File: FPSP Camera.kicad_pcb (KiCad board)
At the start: 4 copper layers, 168.1 x 35 mm, 81 parts, among them J2 Conn_01x02_Pin, J3 USB_B_Micro, J4 SM03B-SRSS-TB, J5 Conn_01x24_Socket, J6 Conn_02x06_Odd_Even, SW1 SW_Push, SW2 SW_Push, U1 RP2350_60QFN, U2 W25Q128JVS, U3 ASM330LHHXTR, U5 TLV74328_SOT23-5, U6 TLV74315_SOT23-5, U7 SiT2001B, U8 NCP1117-3.3_SOT223

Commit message: pcb update
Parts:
- moved D2 19.7 mm to (22.7, 32.2), turned to 0 degrees
- moved D3 17.8 mm to (22.7, 35.2), turned to 0 degrees
- moved C15 16.8 mm to (85.9, 27.2), turned to 90 degrees
- moved J4 16.5 mm to (85.5, 46.5)
- moved TP2 14.5 mm to (82.7, 22.5)
- moved R20 14.4 mm to (26.0, 32.2), turned to 180 degrees
- moved J6 13.9 mm to (48.0, 45.5), turned to -90 degrees
- moved D1 13.8 mm to (22.8, 29.2), turned to 0 degrees
- moved R21 12.7 mm to (26.0, 35.2), turned to 180 degrees
- moved TP1 12.4 mm to (65.7, 44.0)
- moved R18 10.9 mm to (26.0, 29.2), turned to 180 degrees
- moved C31 10.3 mm to (30.7, 37.9)
- moved R2 9.57 mm to (74.7, 17.2)
- moved R6 9.50 mm to (76.4, 17.2)
- moved C14 9.16 mm to (71.9, 36.5), turned to 180 degrees
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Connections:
- U1 pad 16: DATA2_1 -> DATA9_1
- U1 pad 17: DATA3_1 -> DATA8_1
- U1 pad 18: DATA4_1 -> DATA7_1
- U1 pad 19: DATA5_1 -> DATA6_1
- U1 pad 27: DATA6_1 -> DATA2_1
- U1 pad 28: DATA7_1 -> DATA5_1
- U1 pad 29: DATA8_1 -> DATA3_1
- U1 pad 31: DATA9_1 -> DATA4_1
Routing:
- net +3.3V: track 0.00 -> 114.9 mm
- net SDO_imu_1: track 0.00 -> 42.0 mm, vias 0 -> 2
- net SDA_imu_1: track 0.00 -> 40.3 mm, vias 0 -> 4
- net INT1_1: track 0.00 -> 35.9 mm
- net /IOs/XCLK: track 0.00 -> 35.6 mm, vias 0 -> 1
- net SCL_imu_1: track 0.00 -> 35.6 mm, vias 0 -> 2
- net DATA4_1: track 0.00 -> 35.0 mm, vias 0 -> 1
- net INT2_1: track 0.00 -> 33.7 mm, vias 0 -> 2
- net CS_1: track 0.00 -> 33.2 mm
- net HSYNC_1: track 0.00 -> 33.1 mm, vias 0 -> 3
- net DATA5_1: track 0.00 -> 33.1 mm, vias 0 -> 1
- net DATA3_1: track 0.00 -> 33.0 mm, vias 0 -> 1
- net DATA2_1: track 0.00 -> 32.7 mm, vias 0 -> 1
- net +2V8: track 0.00 -> 27.5 mm, vias 0 -> 2
- net DATA6_1: track 0.00 -> 26.9 mm, vias 0 -> 1
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- added copper zone on F.Cu, net +3.3V
- added copper zone on F.Cu, net +5V
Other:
- board text added: "1.5"
- board text added: "2.8"
- board text added: "3.3"
- board text added: "5.0"

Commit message: finished the routing
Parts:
- removed C17: 100n, Capacitor_SMD:C_0603_1608Metric_Pad1.08x0.95mm_HandSolder
- moved J6 12.9 mm to (35.5, 48.2), turned to 90 degrees
- moved TP1 0.50 mm to (65.7, 43.5)
- moved TP2 0.50 mm to (82.7, 23.0)
- moved C21 0.40 mm to (56.0, 38.8)
- moved R13 0.40 mm to (56.0, 36.8)
- moved J3 0.31 mm to (91.0, 16.9)
- moved C35 0.25 mm to (56.0, 40.8)
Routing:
- net +3.3V: track 114.9 -> 266.2 mm, vias 0 -> 12
- net POSITION_OUT_1: track 0.00 -> 58.9 mm, vias 0 -> 1
- net IMAGE_OUT_1_1: track 0.00 -> 58.5 mm, vias 0 -> 1
- net IMAGE_OUT_2_1: track 0.00 -> 57.4 mm, vias 0 -> 1
- net /MCU/FLASH_SS_1: track 12.7 -> 32.1 mm, vias 0 -> 2
- net +1V1: track 26.7 -> 44.6 mm
- net +1V5: track 21.2 -> 37.1 mm, vias 2 -> 3
- net +2V8: track 27.5 -> 43.2 mm, vias 2 -> 3
- net /MCU/QSPI_SS_1: track 1.70 -> 15.7 mm, vias 0 -> 2
- net ~{RESET_1}: track 20.5 -> 25.7 mm, vias 1 -> 2
- net /IOs/PWDN_1: track 0.00 -> 5.12 mm, vias 0 -> 1
- net DATA1_1: track 0.00 -> 5.09 mm, vias 0 -> 1
- net PCLK_1: track 22.0 -> 26.0 mm, vias 1 -> 2
- net Net-(J5-Pin_1): track 0.00 -> 3.98 mm, vias 0 -> 1
- net DATA5_1: track 33.1 -> 30.7 mm
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- added copper zone on B.Cu, net GND
- added copper zone on F.Cu, net GND

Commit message: layout details finalized for prototype
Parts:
- moved H3 82.6 mm to (99.9, 46.5)
- moved H2 82.2 mm to (99.8, 18.5)
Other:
- board size 168.1 x 35 mm -> 85.7 x 35 mm
- board text added: "FPSP v1.0 Junyuan Zheng Junzhe Chen"
- board text added: "GND"
- board text added: "Img1|Img2|Pos"
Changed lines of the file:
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@@
 		(tags "capacitor handsolder")
 		(property "Reference" "C35"
-			(at 3.4375 -0.05 0)
+			(at 3.2375 -0.2 0)
 			(layer "F.SilkS")
 			(effects
@@
 	(footprint "MountingHole:MountingHole_2.7mm_M2.5"
 		(layer "F.Cu")
-		(at 182.45 46.6)
+		(at 99.9 46.5)
 		(descr "Mounting Hole 2.7mm, M2.5, no annular, generated by kicad-footprint-generator mountinghole.py")
 		(tags "mountinghole M2.5")
@@
 	(footprint "MountingHole:MountingHole_2.7mm_M2.5"
 		(layer "F.Cu")
-		(at 181.95 18.9)
+		(at 99.8 18.5)
 		(descr "Mounting Hole 2.7mm, M2.5, no annular, generated by kicad-footprint-generator mountinghole.py")
 		(tags "mountinghole M2.5")
@@
 		(tags "capacitor handsolder")
 		(property "Reference" "C30"
-			(at 0 -2.9 90)
+			(at 0 -1.7125 90)
 			(layer "F.SilkS")
 			(effects
@@
 		(tags "Through hole pin header THT 2x06 2.54mm double row")
 		(property "Reference" "J6"
-			(at 1.27 -2.38 90)
+			(at 0.9 15.35 90)
 			(layer "F.SilkS")
+			(hide yes)
 			(effects
 				(font
@@
 			(at 0 0 0)
 			(layer "F.SilkS")
+			(hide yes)
 			(effects
 				(font
@@
 			(at 0 0 270)
 			(layer "F.SilkS")
+			(hide yes)
 			(effects
 				(font
@@
 		)
 	)
+	(gr_line
+		(start 47.25 43)
+		(end 38.3 44.05)
+		(stroke
+			(width 0.13)
+			(type solid)
+		)
+		(layer "F.SilkS")
+	)
+	(gr_line
+		(start 51.3 42.85)
+		(end 40.65 44.1)
+		(stroke
+			(width 0.13)
+			(type solid)
+		)
+		(layer "F.SilkS")
+	)
+	(gr_line
+		(start 43.35 42.85)
+		(end 35.55 44.1)
+		(stroke
+			(width 0.13)
+			(type solid)
+		)
+		(layer "F.SilkS")
+	)
 	(gr_rect
 		(start 17.7 15)
-		(end 185.848 50)
+		(end 103.424 50)
 		(stroke
 			(width 0.2)
@@
 		(layer "Edge.Cuts")
 	)
+	(gr_text "Img1|Img2|Pos"
+		(at 42.9 42.7 0)
+		(layer "F.SilkS")
+		(effects
+			(font
+				(size 0.8 0.8)
+				(thickness 0.15)
+				(bold yes)
+			)
+			(justify left bottom)
+		)
+	)
 	(gr_text "1.5"
 		(at 17.88 35.95 0)
@@
 		)
 	)
+	(gr_text "GND"
+		(at 50.1 46.2 0)
+		(layer "F.SilkS")
+		(effects
+			(font
+				(size 0.8 0.8)
+				(thickness 0.15)
+				(bold yes)
+			)
+			(justify left bottom)
+		)
+	)
 	(gr_text "1V1"
 		(at 78.7 23 0)
@@
 		)
 	)
+	(gr_text "FPSP v1.0\nJunyuan Zheng\nJunzhe Chen\n"
+		(at 101.65 38.9 90)
+		(layer "F.SilkS")
+		(effects
+			(font
+				(size 1 1)
+				(thickness 0.25)
+				(bold yes)
+			)
+			(justify left bottom)
+		)
+	)
 	(gr_text "3.3"
 		(at 17.98 29.95 0)
@@
 		(polygon
 			(pts
-				(xy 17.7 15) (xy 17.7 50) (xy 96.7 50) (xy 96.7 15)
+				(xy 17.7 15) (xy 17.7 50) (xy 103.426 50) (xy 103.426 15)
 			)
 		)

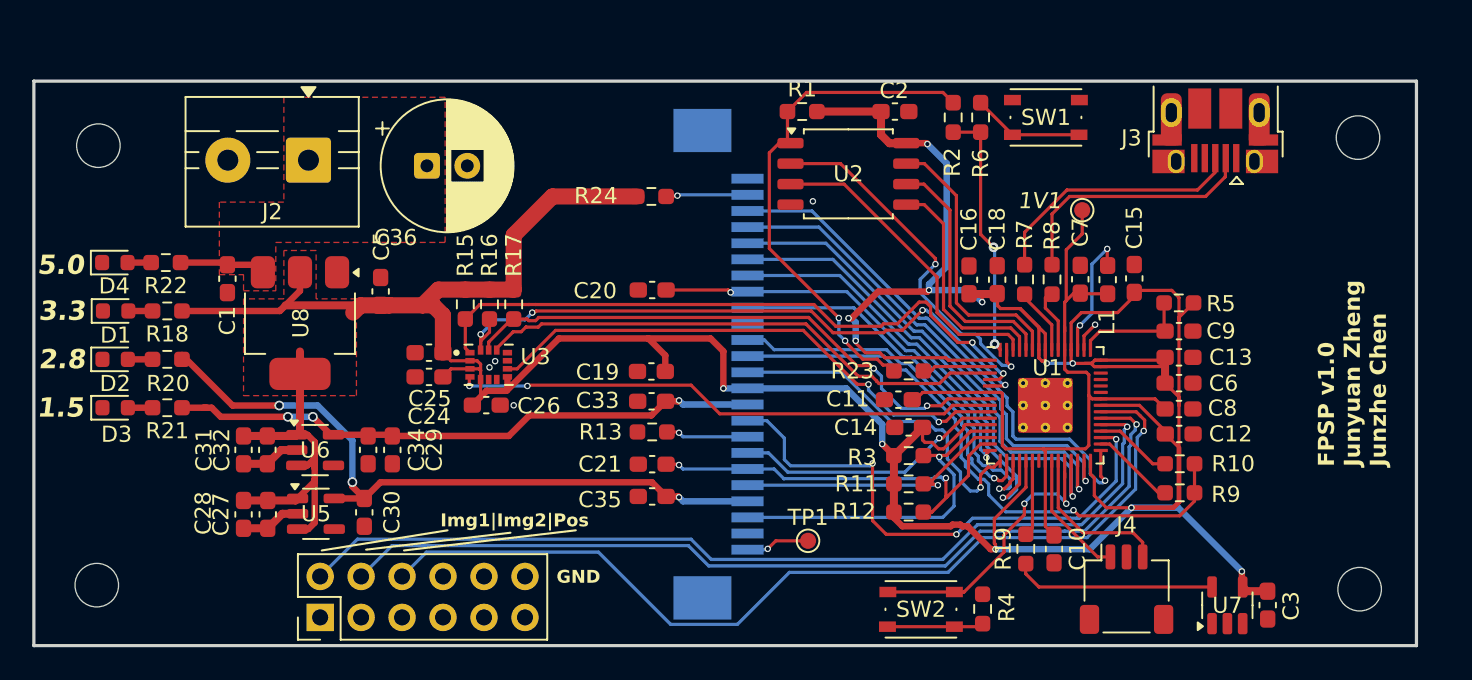
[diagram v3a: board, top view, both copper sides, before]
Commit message: vital change to pin order of connector; RP2350 SMPS layout changed
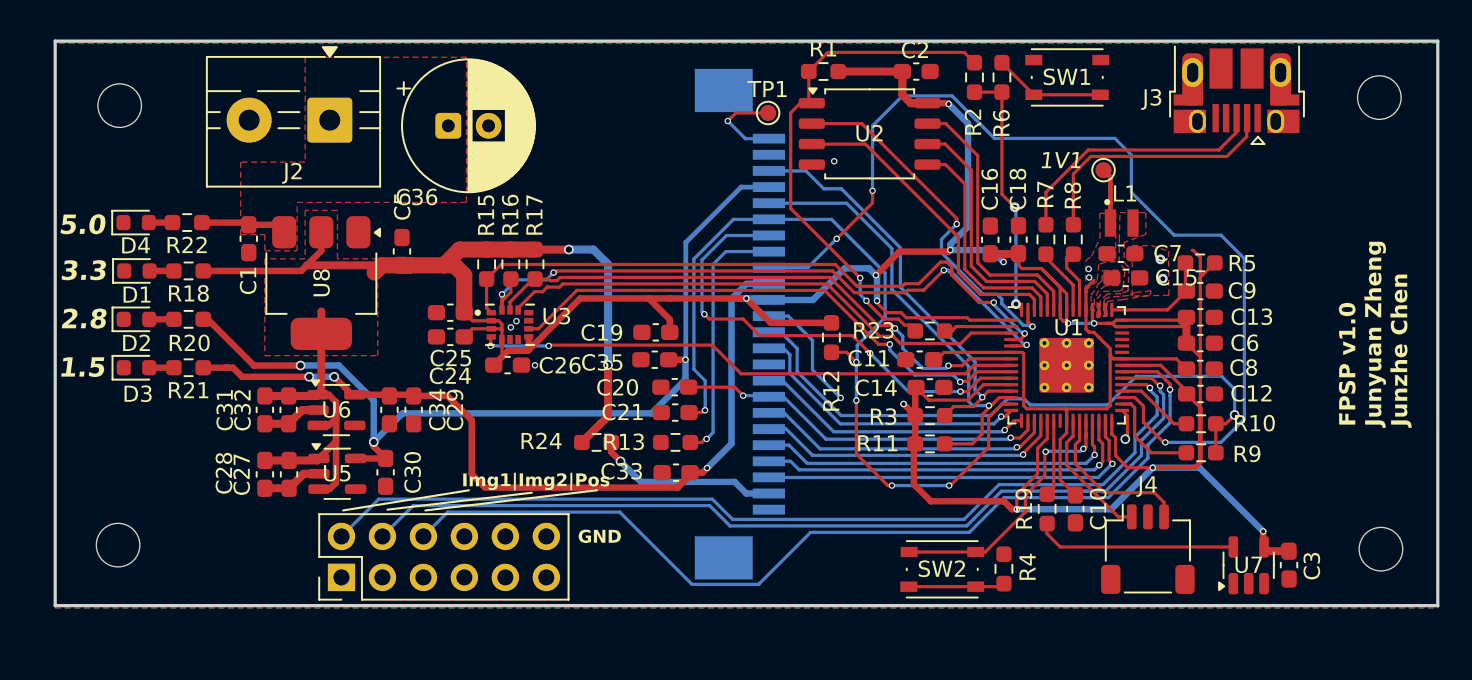
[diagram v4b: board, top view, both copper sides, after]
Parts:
- L1: footprint Inductor_SMD:L_0603_1608Metric_Pad1.05x0.95mm_HandSolder -> RP2350_60QFN_minimal:L_pol_2016
- moved TP1 26.6 mm to (63.2, 17.0)
- moved R24 15.6 mm to (52.6, 37.4)
- moved R12 11.8 mm to (67.2, 30.9), turned to -90 degrees
- moved C35 8.48 mm to (56.2, 32.3)
- moved C20 6.19 mm to (57.4, 34.0)
- moved C33 4.68 mm to (57.5, 39.3)
- moved L1 3.62 mm to (85.2, 23.8), turned to 0 degrees
- moved C21 3.50 mm to (57.5, 35.5)
- moved C7 2.98 mm to (85.1, 25.7), turned to 0 degrees
- moved C11 2.81 mm to (72.6, 32.3)
- moved C14 2.81 mm to (73.3, 34.0), turned to 0 degrees
- moved C6 2.81 mm to (90.0, 31.2)
- moved C8 2.81 mm to (90.0, 32.8)
- moved D3 2.81 mm to (24.1, 32.8)
- moved J4 2.81 mm to (86.8, 44.0)
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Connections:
- J5 pad 1: Net-(J5-Pin_1) -> /IOs/DATA0_1
- J5 pad 10: +1V5 -> GND
- J5 pad 11: +3.3V -> DATA8_1
- J5 pad 12: DATA9_1 -> /IOs/XCLK
- J5 pad 13: /IOs/XCLK -> DATA9_1
- J5 pad 14: DATA8_1 -> +3.3V
- J5 pad 15: GND -> +1V5
- J5 pad 16: DATA7_1 -> HSYNC_1
- J5 pad 17: PCLK_1 -> /IOs/PWDN_1
- J5 pad 18: DATA6_1 -> VSYNC_1
- J5 pad 19: DATA2_1 -> ~{RESET_1}
- J5 pad 2: GND -> DATA1_1
- J5 pad 20: DATA5_1 -> SCL_cam_1
- J5 pad 21: DATA3_1 -> +2V8
- J5 pad 22: DATA4_1 -> SDA_cam_1
- J5 pad 23: DATA1_1 -> GND
- J5 pad 24: /IOs/DATA0_1 -> Net-(J5-Pin_24)
- J5 pad 3: SDA_cam_1 -> DATA4_1
- J5 pad 4: +2V8 -> DATA3_1
- J5 pad 5: SCL_cam_1 -> DATA5_1
- J5 pad 6: ~{RESET_1} -> DATA2_1
- J5 pad 7: VSYNC_1 -> DATA6_1
- J5 pad 8: /IOs/PWDN_1 -> PCLK_1
- J5 pad 9: HSYNC_1 -> DATA7_1
- TP1 pad 1: Net-(J5-Pin_1) -> Net-(J5-Pin_24)
- U1 pad 15: PCLK_1 -> DATA8_1
- U1 pad 16: DATA9_1 -> DATA7_1
- U1 pad 17: DATA8_1 -> PCLK_1
- U1 pad 18: DATA7_1 -> DATA6_1
- U1 pad 19: DATA6_1 -> DATA2_1
- U1 pad 27: DATA2_1 -> DATA5_1
- U1 pad 28: DATA5_1 -> DATA3_1
- U1 pad 29: DATA3_1 -> DATA4_1
- U1 pad 31: DATA4_1 -> DATA9_1
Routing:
- net HSYNC_1: track 33.7 -> 62.0 mm
- net ~{RESET_1}: track 25.7 -> 52.3 mm, vias 2 -> 5
- net +1V5: track 37.1 -> 50.8 mm
- net +2V8: track 43.2 -> 56.5 mm
- net VSYNC_1: track 16.9 -> 29.6 mm, vias 1 -> 3
- net DATA9_1: track 21.2 -> 9.54 mm, vias 1 -> 2
- net DATA2_1: track 30.6 -> 19.0 mm
- net /IOs/PWDN_1: track 5.12 -> 15.9 mm
- net SCL_cam_1: track 18.2 -> 27.8 mm
- net DATA6_1: track 27.7 -> 18.5 mm
- net DATA4_1: track 32.9 -> 24.5 mm
- net DATA7_1: track 25.5 -> 17.3 mm
- net /MCU/VREG_LX_1: track 8.09 -> 0.00 mm, vias 2 -> 0
- net DATA5_1: track 30.7 -> 23.1 mm
- net +1V1: track 44.6 -> 37.8 mm, vias 0 -> 2
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- added copper zone on F.Cu, net +1V1
- added copper zone on F.Cu, net /MCU/VREG_LX_1

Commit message: Cleanup
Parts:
- removed C1, C19, C25, C27, C28, C30, C31, C32, C33, C34, C35, C5: 10u, Capacitor_SMD:C_0603_1608Metric_Pad1.08x0.95mm_HandSolder
- removed C10, C6, C7, C9: 4.7u, Capacitor_SMD:C_0603_1608Metric_Pad1.08x0.95mm_HandSolder
- removed C11, C12, C13, C14, C15, C16, C18, C2, C24, C26, C8: 100n, Capacitor_SMD:C_0603_1608Metric_Pad1.08x0.95mm_HandSolder
- removed C20: 22pF, Capacitor_SMD:C_0603_1608Metric_Pad1.08x0.95mm_HandSolder
- removed C21: 0.1u, Capacitor_SMD:C_0603_1608Metric_Pad1.08x0.95mm_HandSolder
- removed C29: 1u, Capacitor_SMD:C_0603_1608Metric_Pad1.08x0.95mm_HandSolder
- removed C3: 100u, Capacitor_SMD:C_0603_1608Metric_Pad1.08x0.95mm_HandSolder
- removed C36: 10u, Capacitor_THT:CP_Radial_D8.0mm_P2.50mm
- removed D1, D2, D3, D4: LED, Diode_SMD:D_0603_1608Metric
- removed H1, H2, H3, H4: MountingHole, MountingHole:MountingHole_2.7mm_M2.5
- removed J2: Conn_01x02_Pin, TerminalBlock:TerminalBlock_MaiXu_MX126-5.0-02P_1x02_P5.00mm
- removed J3: USB_B_Micro, RP2350_60QFN_minimal:USB_Micro-B_Amphenol_10103594-0001LF_Horizontal_modified
- removed J4: SM03B-SRSS-TB, Connector_JST:JST_SH_SM03B-SRSS-TB_1x03-1MP_P1.00mm_Horizontal
- removed J5: Conn_01x24_Socket, Connector_FFC-FPC:TE_2-84952-4_1x24-1MP_P1.0mm_Horizontal
- removed J6: Conn_02x06_Odd_Even, Connector_PinHeader_2.54mm:PinHeader_2x06_P2.54mm_Vertical
- removed L1: 3.3u, RP2350_60QFN_minimal:L_pol_2016
- removed R1, R19, R23: DNF, Resistor_SMD:R_0603_1608Metric_Pad0.98x0.95mm_HandSolder
- removed R10, R24, R9: 0R, Resistor_SMD:R_0603_1608Metric_Pad0.98x0.95mm_HandSolder
- removed R11, R12, R13, R15, R16, R17, R18, R20, R21, R22, R3: 10k, Resistor_SMD:R_0603_1608Metric_Pad0.98x0.95mm_HandSolder
- removed R2: 0, Resistor_SMD:R_0603_1608Metric_Pad0.98x0.95mm_HandSolder
- removed R4, R6: 1k, Resistor_SMD:R_0603_1608Metric_Pad0.98x0.95mm_HandSolder
- removed R5: 33, Resistor_SMD:R_0603_1608Metric_Pad0.98x0.95mm_HandSolder
- removed R7, R8: 27, Resistor_SMD:R_0603_1608Metric_Pad0.98x0.95mm_HandSolder
- removed SW1, SW2: SW_Push, Button_Switch_SMD:SW_Push_1P1T_NO_Vertical_Wuerth_434133025816
- removed TP1, TP2: TestPoint, TestPoint:TestPoint_Pad_D1.0mm
- removed U1: RP2350_60QFN, RP2350_60QFN_minimal:RP2350-QFN-60-1EP_7x7_P0.4mm_EP3.4x3.4mm_ThermalVias
- removed U2: W25Q128JVS, Package_SO:SOIC-8_5.3x5.3mm_P1.27mm
- removed U3: ASM330LHHXTR, ASM330LHHXTR:XDCR_ASM330LHHXTR
- removed U5: TLV74328_SOT23-5, Package_TO_SOT_SMD:SOT-23-5
- removed U6: TLV74315_SOT23-5, Package_TO_SOT_SMD:SOT-23-5
- removed U7: SiT2001B, Package_TO_SOT_SMD:SOT-23-5
- removed U8: NCP1117-3.3_SOT223, Package_TO_SOT_SMD:SOT-223-3_TabPin2
- added C101: 100n, Capacitor_SMD:C_0603_1608Metric_Pad1.08x0.95mm_HandSolder, F.Cu at (74.8, 28.9)
- added C102: 4.7u, Capacitor_SMD:C_0603_1608Metric_Pad1.08x0.95mm_HandSolder, F.Cu at (59.1, 28.7)
- added C103: 100n, Capacitor_SMD:C_0603_1608Metric_Pad1.08x0.95mm_HandSolder, F.Cu at (66.9, 38.1)
- added C106: 100n, Capacitor_SMD:C_0603_1608Metric_Pad1.08x0.95mm_HandSolder, F.Cu at (74.8, 30.4)
- added C107: 100n, Capacitor_SMD:C_0603_1608Metric_Pad1.08x0.95mm_HandSolder, F.Cu at (74.8, 27.4)
- added C108: 100n, Capacitor_SMD:C_0603_1608Metric_Pad1.08x0.95mm_HandSolder, F.Cu at (74.8, 25.9)
- added C109: 100n, Capacitor_SMD:C_0603_1608Metric_Pad1.08x0.95mm_HandSolder, F.Cu at (71.4, 22.6)
- added C110: 100n, Capacitor_SMD:C_0603_1608Metric_Pad1.08x0.95mm_HandSolder, F.Cu at (69.9, 22.6)
- added C111: 100n, Capacitor_SMD:C_0603_1608Metric_Pad1.08x0.95mm_HandSolder, F.Cu at (65.4, 22.6)
- added C112: 100n, Capacitor_SMD:C_0603_1608Metric_Pad1.08x0.95mm_HandSolder, F.Cu at (70.4, 38.0)
- added C113: 100n, Capacitor_SMD:C_0603_1608Metric_Pad1.08x0.95mm_HandSolder, F.Cu at (63.4, 38.1)
- added C114: 100n, Capacitor_SMD:C_0603_1608Metric_Pad1.08x0.95mm_HandSolder, F.Cu at (59.1, 31.7)
- added C115: 100n, Capacitor_SMD:C_0603_1608Metric_Pad1.08x0.95mm_HandSolder, F.Cu at (59.1, 27.2)
- added C116: 4.7u, Capacitor_SMD:C_0603_1608Metric_Pad1.08x0.95mm_HandSolder, F.Cu at (77.4, 22.4)
- added C117: 4.7u, Capacitor_SMD:C_0603_1608Metric_Pad1.08x0.95mm_HandSolder, F.Cu at (79.9, 20.2)
- added C118: 4.7u, Capacitor_SMD:C_0603_1608Metric_Pad1.08x0.95mm_HandSolder, F.Cu at (75.3, 20.4)
- added C120: 0.1u, Capacitor_SMD:C_0603_1608Metric_Pad1.08x0.95mm_HandSolder, F.Cu at (46.7, 36.8)
- added C121: 22pF, Capacitor_SMD:C_0603_1608Metric_Pad1.08x0.95mm_HandSolder, F.Cu at (47.0, 25.8)
- added C122: 100n, Capacitor_SMD:C_0603_1608Metric_Pad1.08x0.95mm_HandSolder, F.Cu at (74.1, 43.9)
- added C123: 1u, Capacitor_SMD:C_0603_1608Metric_Pad1.08x0.95mm_HandSolder, F.Cu at (36.8, 21.9)
- added C124: 1u, Capacitor_SMD:C_0603_1608Metric_Pad1.08x0.95mm_HandSolder, F.Cu at (31.8, 21.9)
- added C125: 1u, Capacitor_SMD:C_0603_1608Metric_Pad1.08x0.95mm_HandSolder, F.Cu at (36.8, 26.3)
- added C126: 1u, Capacitor_SMD:C_0603_1608Metric_Pad1.08x0.95mm_HandSolder, F.Cu at (32.0, 26.4)
- added C127: 1u, Capacitor_SMD:C_0603_1608Metric_Pad1.08x0.95mm_HandSolder, F.Cu at (36.6, 30.9)
- added C128: 1u, Capacitor_SMD:C_0603_1608Metric_Pad1.08x0.95mm_HandSolder, F.Cu at (31.9, 30.9)
- added D101: LED, Diode_SMD:D_0603_1608Metric, F.Cu at (24.2, 22.0)
- added D102: LED, Diode_SMD:D_0603_1608Metric, F.Cu at (24.2, 25.0)
- added D103: LED, Diode_SMD:D_0603_1608Metric, F.Cu at (24.2, 28.0)
- added D104: LED, Diode_SMD:D_0603_1608Metric, F.Cu at (24.2, 31.0)
- added H101: MountingHole, MountingHole:MountingHole_2.7mm_M2.5, F.Cu at (22.3, 15.8)
- added H102: MountingHole, MountingHole:MountingHole_2.7mm_M2.5, F.Cu at (22.3, 44.3)
- added H103: MountingHole, MountingHole:MountingHole_2.7mm_M2.5, F.Cu at (101.5, 44.0)
- added H104: MountingHole, MountingHole:MountingHole_2.7mm_M2.5, F.Cu at (101.5, 15.8)
- added J101: Conn_01x24_Socket, Connector_FFC-FPC:TE_2-84952-4_1x24-1MP_P1.0mm_Horizontal, B.Cu at (48.1, 30.2)
- added JP101: SolderJumper_2_Open, Jumper:SolderJumper-2_P1.3mm_Open_RoundedPad1.0x1.5mm, F.Cu at (63.4, 15.9)
- added JP102: SolderJumper_2_Open, Jumper:SolderJumper-2_P1.3mm_Open_RoundedPad1.0x1.5mm, F.Cu at (65.3, 44.7)
- added L101: 3.3u, Inductor_SMD:L_1210_3225Metric, F.Cu at (75.8, 17.2)
- added R104: 33, Resistor_SMD:R_0603_1608Metric_Pad0.98x0.95mm_HandSolder, F.Cu at (80.6, 16.7)
- added R105: 27, Resistor_SMD:R_0603_1608Metric_Pad0.98x0.95mm_HandSolder, F.Cu at (66.9, 22.6)
- added R106: 27, Resistor_SMD:R_0603_1608Metric_Pad0.98x0.95mm_HandSolder, F.Cu at (68.4, 22.6)
- added R108: 1k, Resistor_SMD:R_0603_1608Metric_Pad0.98x0.95mm_HandSolder, F.Cu at (63.9, 22.5)
- added R111: 10k, Resistor_SMD:R_0603_1608Metric_Pad0.98x0.95mm_HandSolder, F.Cu at (46.7, 39.8)
- added R112: 10k, Resistor_SMD:R_0603_1608Metric_Pad0.98x0.95mm_HandSolder, F.Cu at (46.7, 38.2)
- added R113: 10k, Resistor_SMD:R_0603_1608Metric_Pad0.98x0.95mm_HandSolder, F.Cu at (46.7, 31.8)
- added R114: DNF, Resistor_SMD:R_0603_1608Metric_Pad0.98x0.95mm_HandSolder, F.Cu at (65.2, 38.1)
- added R115: 0R, Resistor_SMD:R_0603_1608Metric_Pad0.98x0.95mm_HandSolder, F.Cu at (47.0, 19.8)
- added R116: 0R, Resistor_SMD:R_0603_1608Metric_Pad0.98x0.95mm_HandSolder, F.Cu at (74.8, 33.4)
- added R117: 10k, Resistor_SMD:R_0603_1608Metric_Pad0.98x0.95mm_HandSolder, F.Cu at (46.7, 34.8)
- added R118: 0R, Resistor_SMD:R_0603_1608Metric_Pad0.98x0.95mm_HandSolder, F.Cu at (74.8, 31.9)
- added R119: 1k, Resistor_SMD:R_0603_1608Metric_Pad0.98x0.95mm_HandSolder, F.Cu at (68.7, 38.0)
- added R120: 0R, Resistor_SMD:R_0603_1608Metric_Pad0.98x0.95mm_HandSolder, F.Cu at (47.0, 27.8)
- added R121: 10k, Resistor_SMD:R_0603_1608Metric_Pad0.98x0.95mm_HandSolder, F.Cu at (27.4, 22.0)
- added R122: 10k, Resistor_SMD:R_0603_1608Metric_Pad0.98x0.95mm_HandSolder, F.Cu at (27.4, 25.0)
- added R123: 10k, Resistor_SMD:R_0603_1608Metric_Pad0.98x0.95mm_HandSolder, F.Cu at (27.4, 28.0)
- added R124: 10k, Resistor_SMD:R_0603_1608Metric_Pad0.98x0.95mm_HandSolder, F.Cu at (27.4, 31.0)
- added TP101: TestPoint, TestPoint:TestPoint_Pad_D1.0mm, F.Cu at (84.3, 17.0)
- added U103: RP2350_60QFN, projLib:RP2350-QFN-60-1EP_7x7_P0.4mm_EP3.4x3.4mm_ThermalVias, F.Cu at (66.9, 30.3)
- added U104: TLV75533PDRV, Package_SON:WSON-6-1EP_2x2mm_P0.65mm_EP1x1.6mm, F.Cu at (34.2, 22.1)
- added U105: TLV73328PDRV, Package_SON:WSON-6-1EP_2x2mm_P0.65mm_EP1x1.6mm, F.Cu at (34.2, 26.4)
- added U106: TLV73315PDRV, Package_SON:WSON-6-1EP_2x2mm_P0.65mm_EP1x1.6mm, F.Cu at (34.1, 30.8)
- added Y101: SiT8008xx-1x-xxE, Oscillator:Oscillator_SMD_SiT_PQFN-4Pin_2.5x2.0mm, F.Cu at (76.7, 43.9)
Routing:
- net +3.3V: track 263.2 -> 5.07 mm, vias 14 -> 0
- net HSYNC_1: track 62.0 -> 0.00 mm, vias 3 -> 0
- net POSITION_OUT_1: track 59.1 -> 0.00 mm, vias 1 -> 0
- net IMAGE_OUT_1_1: track 59.0 -> 0.00 mm, vias 1 -> 0
- net IMAGE_OUT_2_1: track 57.7 -> 0.00 mm, vias 1 -> 0
- net ~{RESET_1}: track 52.3 -> 0.00 mm, vias 5 -> 0
- net +2V8: track 56.5 -> 4.68 mm, vias 3 -> 0
- net +1V5: track 50.8 -> 3.90 mm, vias 3 -> 0
- net SDO_imu_1: track 40.4 -> 0.00 mm, vias 2 -> 0
- net SDA_imu_1: track 40.2 -> 0.00 mm, vias 4 -> 0
- net /IOs/XCLK: track 38.3 -> 0.00 mm, vias 1 -> 0
- net +1V1: track 37.8 -> 0.00 mm, vias 2 -> 0
- net SCL_imu_1: track 35.3 -> 0.00 mm, vias 2 -> 0
- net INT1_1: track 33.8 -> 0.00 mm, vias 2 -> 0
- net INT2_1: track 33.7 -> 0.00 mm, vias 2 -> 0
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- added copper zone on B.Cu, net (none)
- added copper zone on F.Cu, net (none)
- added copper zone on F.Cu, net +1V5
- added copper zone on F.Cu, net +2V8
- added copper zone on F.Cu, net AGND
- removed copper zone on F.Cu, net +1V1
- removed copper zone on F.Cu, net /MCU/VREG_LX_1
- removed copper zone on B.Cu, net GND
- removed copper zone on F.Cu, net GND
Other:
- board text added: "VDD"
- board text removed: "1V1"
- board text removed: "5.0"
- board text removed: "FPSP v1.0 Junyuan Zheng Junzhe Chen"
- board text removed: "GND"
- board text removed: "Img1|Img2|Pos"
